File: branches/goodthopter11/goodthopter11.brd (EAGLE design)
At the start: 73 x 35.6 mm, 24 parts, among them IC1 F22X4---DA38, IC2 FT232RL-BASICSSOP, Q2 20MHz

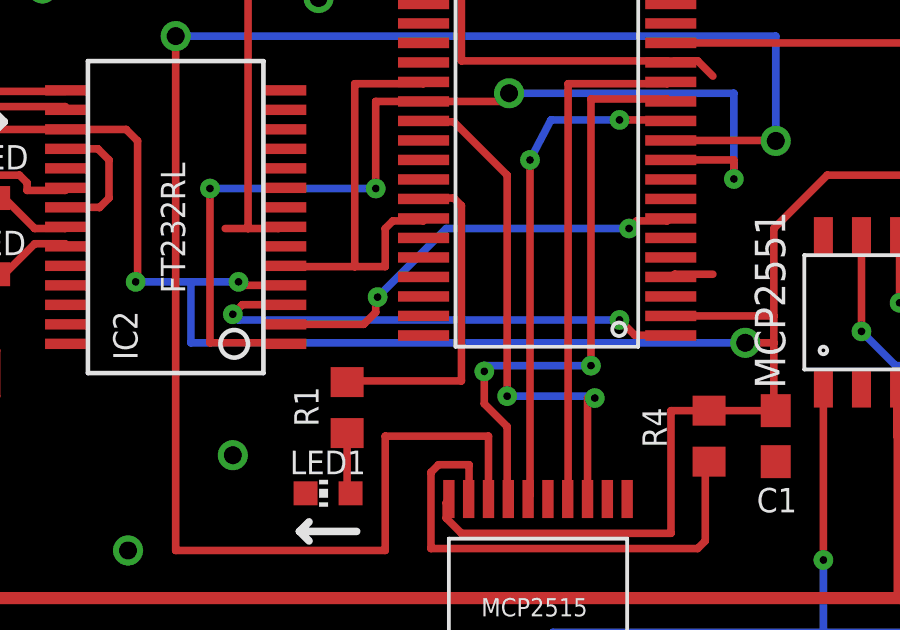
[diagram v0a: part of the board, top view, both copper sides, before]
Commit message: Moved via away from IC in GT11.
git-svn-id: https://svn.code.sf.net/p/goodfet/code@1293 12e2690d-a6be-4b82-a7b7-67c4a43b65c8
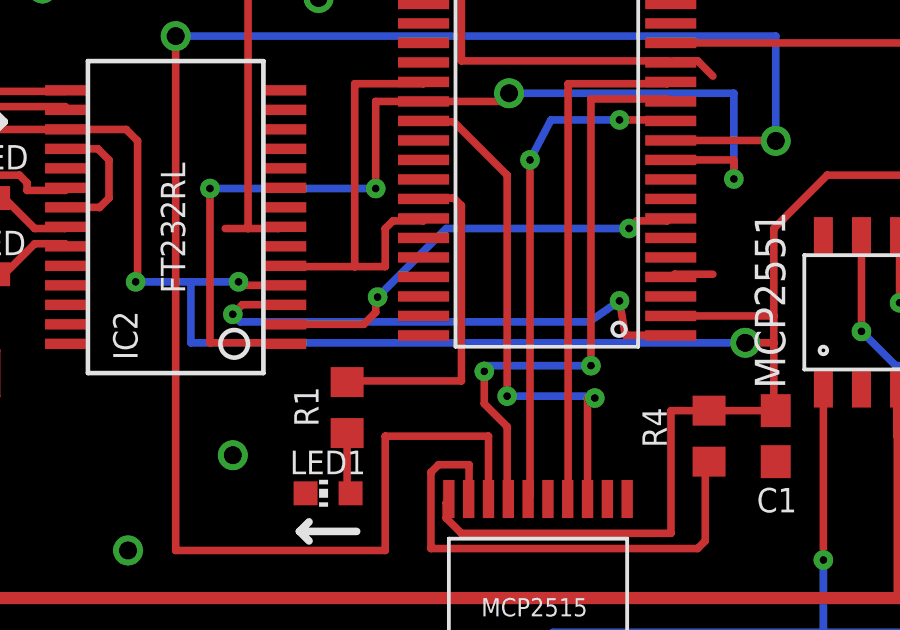
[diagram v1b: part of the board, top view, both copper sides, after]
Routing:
- net RTS: track 16.8 -> 17.8 mm
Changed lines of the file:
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@@
 <setting verticaltext="up"/>
 </settings>
-<grid distance="0.0125" unitdist="inch" unit="inch" style="lines" multiple="1" display="no" altdistance="0.025" altunitdist="inch" altunit="inch"/>
+<grid distance="0.0125" unitdist="inch" unit="inch" style="lines" multiple="1" display="no" altdistance="0.0001" altunitdist="inch" altunit="inch"/>
 <layers>
 <layer number="1" name="Top" color="4" fill="1" visible="yes" active="yes"/>
@@
 <contactref element="IC2" pad="3"/>
 <contactref element="IC1" pad="1"/>
-<wire x1="38.2905" y1="20.3835" x2="25.5905" y2="20.3835" width="0.254" layer="16"/>
-<wire x1="39.878" y1="19.8755" x2="38.7985" y2="19.8755" width="0.254" layer="1"/>
+<wire x1="38.2905" y1="21.0185" x2="37.2745" y2="20.32" width="0.254" layer="16"/>
+<wire x1="39.878" y1="19.8755" x2="38.481" y2="19.8755" width="0.254" layer="1"/>
 <wire x1="27.178" y1="20.8915" x2="27.151" y2="20.8875" width="0.254" layer="1"/>
 <wire x1="39.878" y1="19.8755" x2="39.9975" y2="19.8675" width="0.254" layer="1"/>
 <via x="25.4" y="20.574" extent="1-16" drill="0.254"/>
-<via x="38.2905" y="20.3835" extent="1-16" drill="0.254"/>
-<wire x1="38.7985" y1="19.8755" x2="38.2905" y2="20.3835" width="0.254" layer="1"/>
+<via x="38.2905" y="21.0185" extent="1-16" drill="0.254"/>
+<wire x1="38.481" y1="19.8755" x2="38.2905" y2="21.0185" width="0.254" layer="1"/>
 <wire x1="27.178" y1="20.8915" x2="25.7175" y2="20.8915" width="0.254" layer="1"/>
 <wire x1="25.7175" y1="20.8915" x2="25.4" y2="20.574" width="0.254" layer="1"/>
-<wire x1="25.5905" y1="20.3835" x2="25.4" y2="20.574" width="0.254" layer="16"/>
+<wire x1="37.2745" y1="20.32" x2="25.654" y2="20.32" width="0.254" layer="16"/>
+<wire x1="25.654" y1="20.32" x2="25.4" y2="20.574" width="0.254" layer="16"/>
 </signal>
 <signal name="DTR">
